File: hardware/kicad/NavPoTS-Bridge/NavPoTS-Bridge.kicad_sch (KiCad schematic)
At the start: 74 parts, among them J1 Conn_01x06_Pin, J2 USB_C_Receptacle_USB2.0_16P, J3 Screw_Terminal_01x06, J4 Conn_02x04_Top_Bottom, J5 Conn_02x04_Top_Bottom, J6 Conn_02x04_Top_Bottom, J7 62684-402100ALF, J8 62684-402100ALF, J9 Conn_02x04_Top_Bottom, U1 MS5611-01BA, U2 H3LIS331DLTR, U3 ASM330LHHXTR, U4 MMC5983MA, U5 USBLC6-2SC6, U6 STM32H743ZITx, Y1 ECS-2520MV-xxx-xx

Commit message: fix mistake in bridge module
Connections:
- net USART3_RX: now also D2.1 (K), R13.1; no longer J3.6 (Pin_6)
- net USART3_TX: now also J3.6 (Pin_6); no longer D2.1 (K), R13.1

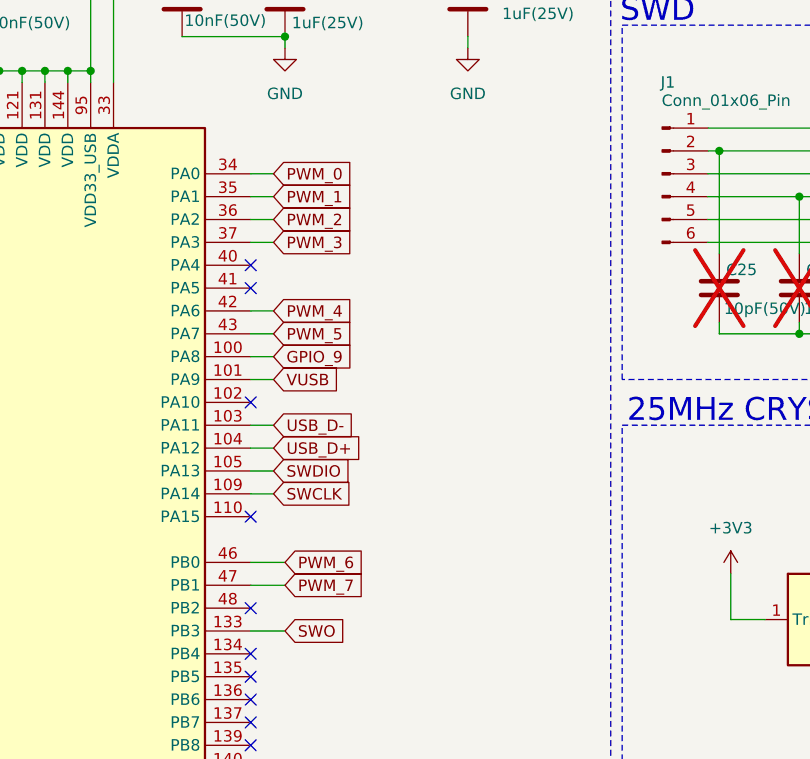
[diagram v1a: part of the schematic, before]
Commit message: added labels next to pwm adc lines
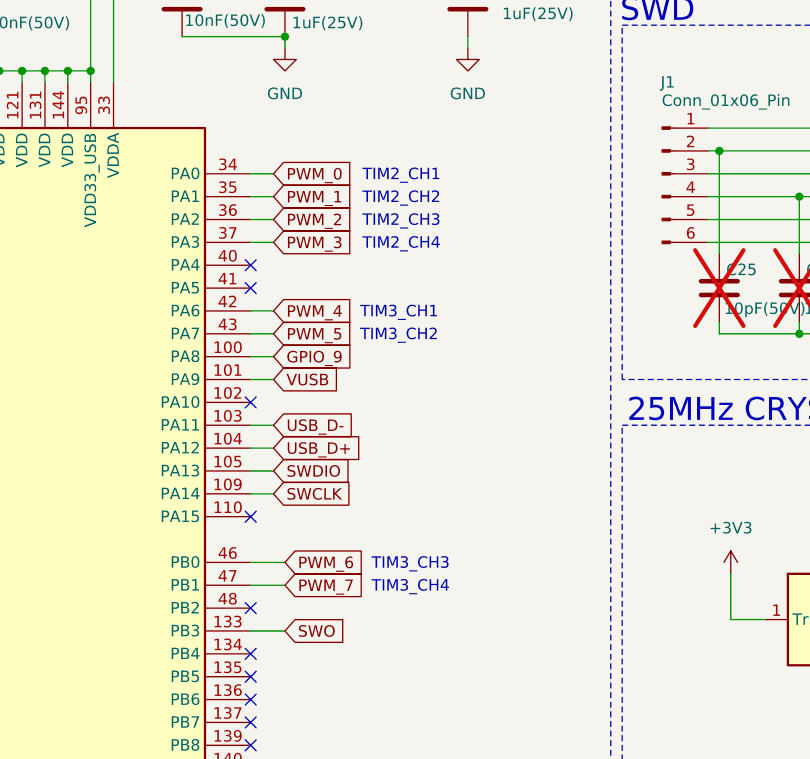
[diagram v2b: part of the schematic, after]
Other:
- note added: "TIM2_CH1"
- note added: "TIM2_CH2"
- note added: "TIM2_CH3"
- note added: "TIM2_CH4"
- note added: "TIM3_CH1"
- note added: "TIM3_CH2"
- note added: "TIM3_CH3"
- note added: "TIM3_CH4"
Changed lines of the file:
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@@
+		)
+	)
+	(text "TIM2_CH2\n"
+		(exclude_from_sim no)
+		(at 214.884 82.804 0)
+		(effects
+			(font
+				(size 1.27 1.27)
+			)
+		)
+	)
+	(text "TIM3_CH1"
+		(exclude_from_sim no)
+		(at 214.63 95.504 0)
+		(effects
+			(font
+				(size 1.27 1.27)
+			)
 		)
 	)
@@
 		)
 	)
+	(text "TIM2_CH4"
+		(exclude_from_sim no)
+		(at 214.884 87.884 0)
+		(effects
+			(font
+				(size 1.27 1.27)
+			)
+		)
+	)
 	(text "MOUNTING HOLES"
 		(exclude_from_sim no)
@@
 		)
 	)
+	(text "TIM2_CH1"
+		(exclude_from_sim no)
+		(at 214.884 80.264 0)
+		(effects
+			(font
+				(size 1.27 1.27)
+			)
+		)
+	)
 	(text "DEBUG\n"
 		(exclude_from_sim no)
@@
 		)
 	)
+	(text "TIM3_CH3"
+		(exclude_from_sim no)
+		(at 215.9 123.444 0)
+		(effects
+			(font
+				(size 1.27 1.27)
+			)
+		)
+	)
 	(text "SOUTH BOARD"
 		(exclude_from_sim no)
@@
 			)
 		)
+	)
+	(text "TIM3_CH4"
+		(exclude_from_sim no)
+		(at 215.9 125.984 0)
+		(effects
+			(font
+				(size 1.27 1.27)
+			)
+		)
+	)
+	(text "TIM2_CH3"
+		(exclude_from_sim no)
+		(at 214.884 85.344 0)
+		(effects
+			(font
+				(size 1.27 1.27)
+			)
+		)
+	)
+	(text "TIM3_CH2"
+		(exclude_from_sim no)
+		(at 214.63 98.044 0)
+		(effects
+			(font
+				(size 1.27 1.27)
+			)
+		)
